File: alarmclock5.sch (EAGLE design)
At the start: 38 parts, among them X1 MKDSN1,5/2-5,08, X2 MKDSN1,5/2-5,08, X3 MKDSN1,5/2-5,08, X4 MKDSN1,5/2-5,08, X5 MKDSN1,5/2-5,08

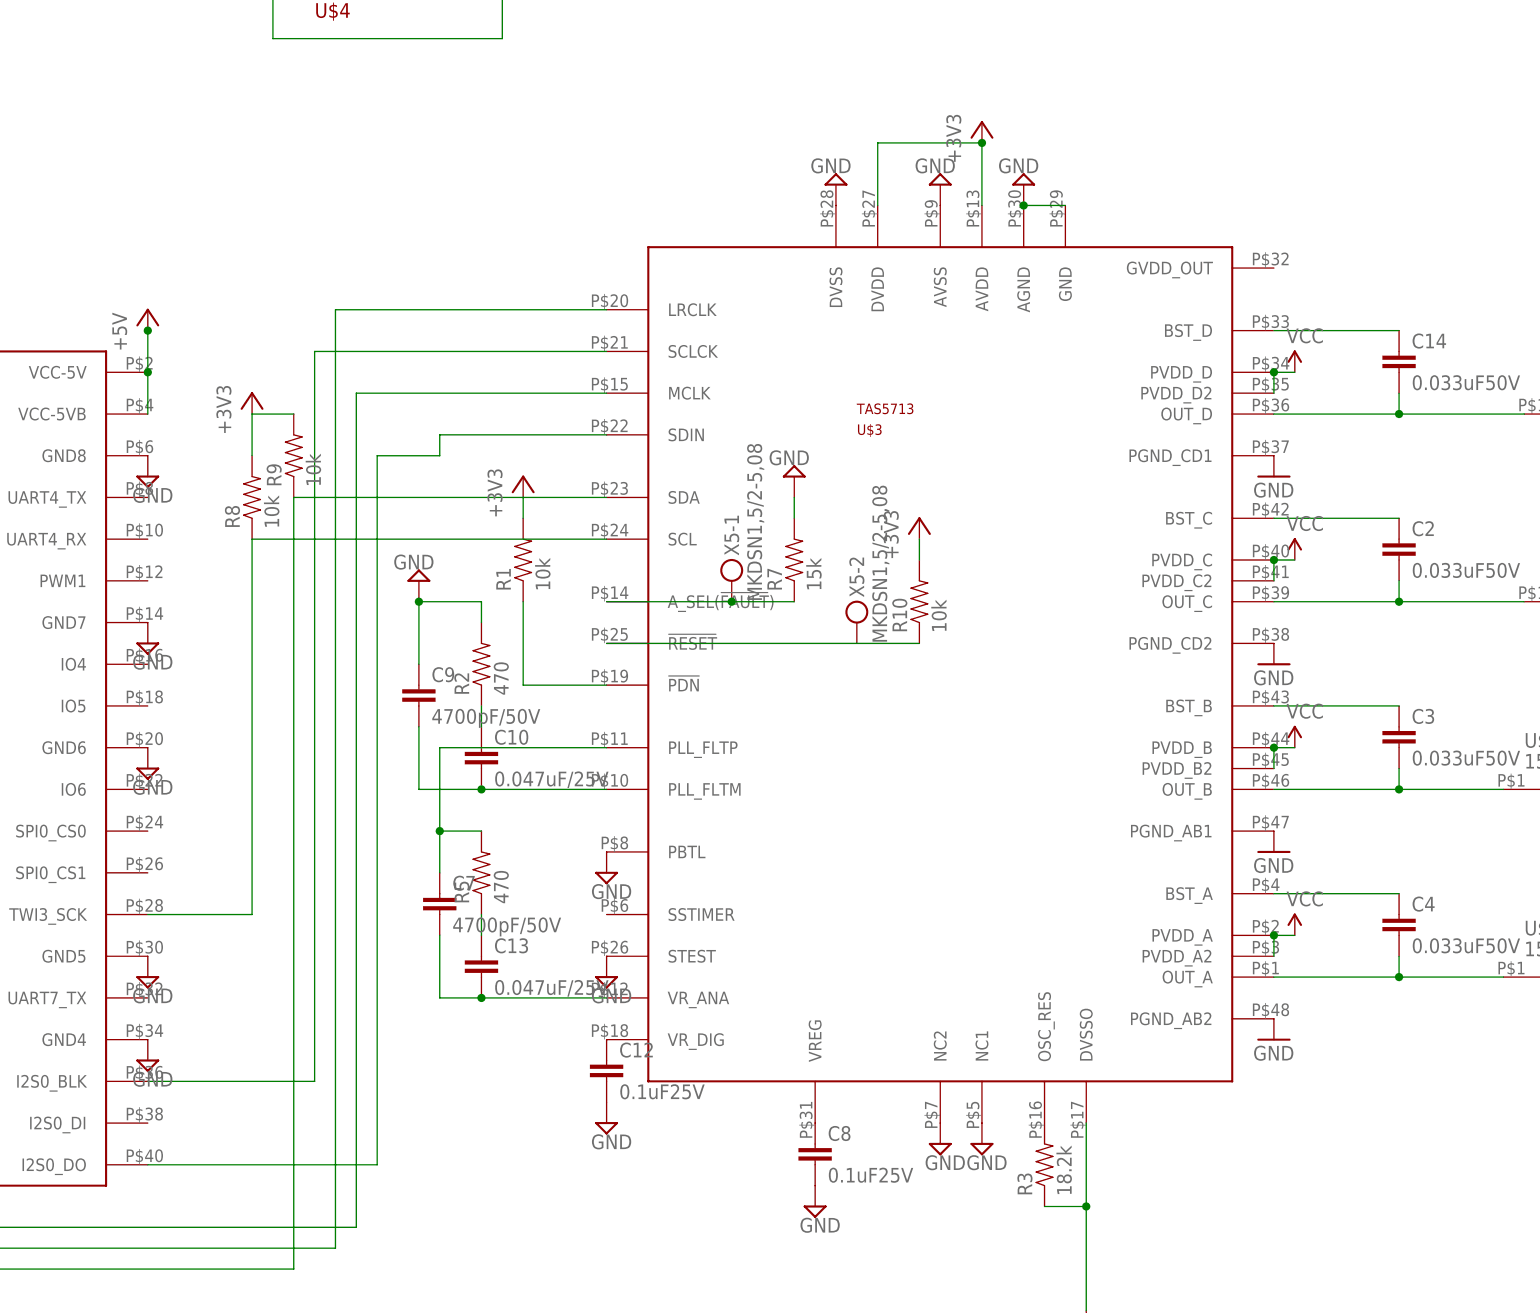
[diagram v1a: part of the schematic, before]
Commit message: new board with RESET and PDN accessible via GPIO
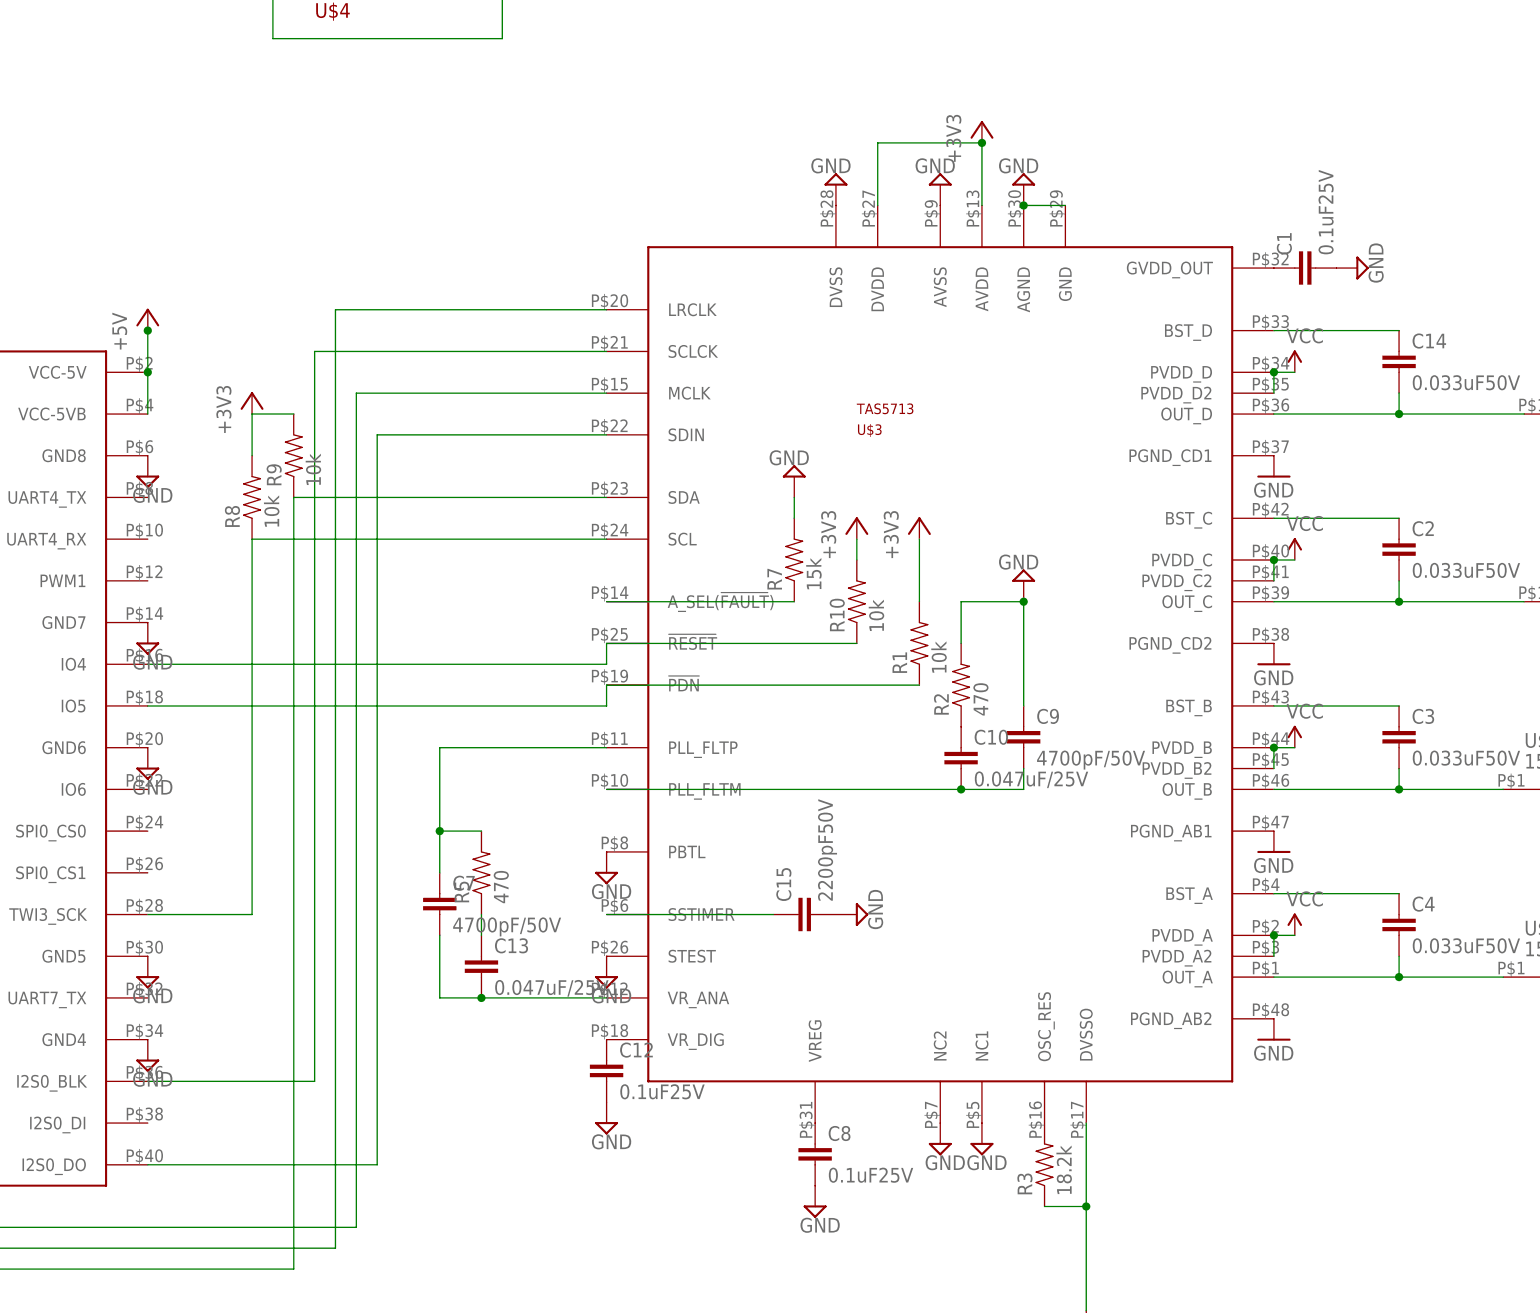
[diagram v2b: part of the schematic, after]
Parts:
- removed X5: MKDSN1,5/2-5,08, con-phoenix-508:MKDSN1,5/2-5,08
- added C1: 0.1uF25V, SparkFun-Capacitors:CAP0603-CAP
- added C15: 2200pF50V, SparkFun-Capacitors:CAP0603-CAP
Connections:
- new net N$38: C1.1, U$3.GVDD_OUT
- new net N$39: C15.1, U$3.SSTIMER
- net GND: now also C1.2, C15.2
- net N$28: now also U$5.IO5
- net N$34: no longer X5-1.KL
- net N$37: now also U$5.IO4; no longer X5-2.KL
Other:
- moved on the sheet: C10, C9, R1, R10, R2
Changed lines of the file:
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@@
 <part name="R9" library="SparkFun-Passives" deviceset="RESISTOR" device="0603-RES" value="10k"/>
 <part name="+3V8" library="supply1" deviceset="+3V3" device=""/>
-<part name="X5" library="con-phoenix-508" deviceset="MKDSN1,5/2-5,08" device=""/>
 <part name="R10" library="SparkFun-Passives" deviceset="RESISTOR" device="0603-RES" value="10k"/>
+<part name="C1" library="SparkFun-Capacitors" deviceset="CAP" device="0603-CAP" value="0.1uF25V"/>
+<part name="SUPPLY18" library="supply2" deviceset="GND" device=""/>
+<part name="C15" library="SparkFun-Capacitors" deviceset="CAP" device="0603-CAP" value="2200pF50V"/>
+<part name="SUPPLY30" library="supply2" deviceset="GND" device=""/>
 </parts>
 <sheets>
@@
 <instance part="C12" gate="G$1" x="76.2" y="-68.58"/>
 <instance part="C13" gate="G$1" x="60.96" y="-55.88"/>
-<instance part="C10" gate="G$1" x="60.96" y="-30.48"/>
+<instance part="C10" gate="G$1" x="119.38" y="-30.48"/>
 <instance part="C7" gate="G$1" x="55.88" y="-48.26"/>
-<instance part="C9" gate="G$1" x="53.34" y="-22.86"/>
+<instance part="C9" gate="G$1" x="127" y="-27.94"/>
 <instance part="R5" gate="G$1" x="60.96" y="-43.18" rot="R90"/>
-<instance part="R2" gate="G$1" x="60.96" y="-17.78" rot="R90"/>
+<instance part="R2" gate="G$1" x="119.38" y="-20.32" rot="R90"/>
 <instance part="R3" gate="G$1" x="129.54" y="-78.74" rot="R90"/>
-<instance part="R1" gate="G$1" x="66.04" y="-5.08" rot="R90"/>
+<instance part="R1" gate="G$1" x="114.3" y="-15.24" rot="R90"/>
 <instance part="C11" gate="G$1" x="73.66" y="76.2"/>
-<instance part="SUPPLY6" gate="GND" x="53.34" y="-7.62" rot="R180"/>
+<instance part="SUPPLY6" gate="GND" x="127" y="-7.62" rot="R180"/>
 <instance part="+3V1" gate="G$1" x="-20.32" y="27.94"/>
 <instance part="P+1" gate="1" x="20.32" y="25.4"/>
-<instance part="+3V2" gate="G$1" x="66.04" y="5.08"/>
+<instance part="+3V2" gate="G$1" x="114.3" y="0"/>
 <instance part="+3V3" gate="G$1" x="121.92" y="48.26"/>
 <instance part="SUPPLY7" gate="GND" x="104.14" y="40.64" rot="R180"/>
@@
 <instance part="SUPPLY25" gate="GND" x="121.92" y="-76.2"/>
 <instance part="SUPPLY26" gate="GND" x="134.62" y="-99.06"/>
-<instance part="+3V4" gate="G$1" x="114.3" y="0"/>
+<instance part="+3V4" gate="G$1" x="106.68" y="0"/>
 <instance part="X3" gate="-1" x="-68.58" y="-7.62" rot="R180"/>
 <instance part="X3" gate="-2" x="-68.58" y="-12.7" rot="R180"/>
@@
 <instance part="R9" gate="G$1" x="38.1" y="7.62" rot="R90"/>
 <instance part="+3V8" gate="G$1" x="33.02" y="15.24"/>
-<instance part="X5" gate="-1" x="91.44" y="-7.62" rot="R90"/>
-<instance part="X5" gate="-2" x="106.68" y="-12.7" rot="R90"/>
-<instance part="R10" gate="G$1" x="114.3" y="-10.16" rot="R90"/>
+<instance part="R10" gate="G$1" x="106.68" y="-10.16" rot="R90"/>
+<instance part="C1" gate="G$1" x="162.56" y="30.48" rot="R90"/>
+<instance part="SUPPLY18" gate="GND" x="167.64" y="30.48" rot="R90"/>
+<instance part="C15" gate="G$1" x="101.6" y="-48.26" rot="R90"/>
+<instance part="SUPPLY30" gate="GND" x="106.68" y="-48.26" rot="R90"/>
 </instances>
 <busses>
@@
 </segment>
 <segment>
-<wire x1="53.34" y1="-17.78" x2="53.34" y2="-10.16" width="0.1524" layer="91"/>
-<wire x1="60.96" y1="-12.7" x2="60.96" y2="-10.16" width="0.1524" layer="91"/>
-<wire x1="60.96" y1="-10.16" x2="53.34" y2="-10.16" width="0.1524" layer="91"/>
+<wire x1="127" y1="-22.86" x2="127" y2="-10.16" width="0.1524" layer="91"/>
+<wire x1="119.38" y1="-15.24" x2="119.38" y2="-10.16" width="0.1524" layer="91"/>
+<wire x1="119.38" y1="-10.16" x2="127" y2="-10.16" width="0.1524" layer="91"/>
 <pinref part="C9" gate="G$1" pin="1"/>
 <pinref part="R2" gate="G$1" pin="2"/>
 <pinref part="SUPPLY6" gate="GND" pin="GND"/>
-<junction x="53.34" y="-10.16"/>
+<junction x="127" y="-10.16"/>
 </segment>
 <segment>
@@
 <wire x1="99.06" y1="0" x2="99.06" y2="2.54" width="0.1524" layer="91"/>
 </segment>
+<segment>
+<pinref part="C1" gate="G$1" pin="2"/>
+<pinref part="SUPPLY18" gate="GND" pin="GND"/>
+</segment>
+<segment>
+<pinref part="C15" gate="G$1" pin="2"/>
+<pinref part="SUPPLY30" gate="GND" pin="GND"/>
+</segment>
 </net>
 <net name="N$1" class="0">
@@
 <pinref part="U$5" gate="G$1" pin="I2S0_DO"/>
 <wire x1="20.32" y1="-78.74" x2="48.26" y2="-78.74" width="0.1524" layer="91"/>
-<wire x1="48.26" y1="-78.74" x2="48.26" y2="7.62" width="0.1524" layer="91"/>
+<wire x1="48.26" y1="-78.74" x2="48.26" y2="10.16" width="0.1524" layer="91"/>
 <pinref part="U$3" gate="G$1" pin="SDIN"/>
-<wire x1="55.88" y1="10.16" x2="76.2" y2="10.16" width="0.1524" layer="91"/>
-<wire x1="55.88" y1="10.16" x2="55.88" y2="7.62" width="0.1524" layer="91"/>
-<wire x1="55.88" y1="7.62" x2="48.26" y2="7.62" width="0.1524" layer="91"/>
+<wire x1="48.26" y1="10.16" x2="76.2" y2="10.16" width="0.1524" layer="91"/>
 </segment>
 </net>
@@
 <segment>
 <pinref part="U$3" gate="G$1" pin="PLL_FLTM"/>
-<wire x1="76.2" y1="-33.02" x2="60.96" y2="-33.02" width="0.1524" layer="91"/>
-<wire x1="60.96" y1="-33.02" x2="53.34" y2="-33.02" width="0.1524" layer="91"/>
-<wire x1="53.34" y1="-25.4" x2="53.34" y2="-33.02" width="0.1524" layer="91"/>
+<wire x1="76.2" y1="-33.02" x2="119.38" y2="-33.02" width="0.1524" layer="91"/>
+<wire x1="119.38" y1="-33.02" x2="127" y2="-33.02" width="0.1524" layer="91"/>
+<wire x1="127" y1="-30.48" x2="127" y2="-33.02" width="0.1524" layer="91"/>
 <pinref part="C10" gate="G$1" pin="2"/>
-<junction x="60.96" y="-33.02"/>
+<junction x="119.38" y="-33.02"/>
 <pinref part="C9" gate="G$1" pin="2"/>
 </segment>
@@
 <net name="N$25" class="0">
 <segment>
-<wire x1="60.96" y1="-22.86" x2="60.96" y2="-25.4" width="0.1524" layer="91"/>
 <pinref part="C10" gate="G$1" pin="1"/>
 <pinref part="R2" gate="G$1" pin="1"/>
@@
 <segment>
 <pinref part="U$3" gate="G$1" pin="!PDN!"/>
-<wire x1="76.2" y1="-20.32" x2="66.04" y2="-20.32" width="0.1524" layer="91"/>
-<wire x1="66.04" y1="-20.32" x2="66.04" y2="-10.16" width="0.1524" layer="91"/>
+<wire x1="76.2" y1="-20.32" x2="114.3" y2="-20.32" width="0.1524" layer="91"/>
 <pinref part="R1" gate="G$1" pin="1"/>
+<pinref part="U$5" gate="G$1" pin="IO5"/>
+<wire x1="20.32" y1="-22.86" x2="76.2" y2="-22.86" width="0.1524" layer="91"/>
+<wire x1="76.2" y1="-22.86" x2="76.2" y2="-20.32" width="0.1524" layer="91"/>
 </segment>
 </net>
@@
 <segment>
 <pinref part="+3V2" gate="G$1" pin="+3V3"/>
-<wire x1="66.04" y1="0" x2="66.04" y2="2.54" width="0.1524" layer="91"/>
+<wire x1="114.3" y1="-10.16" x2="114.3" y2="-2.54" width="0.1524" layer="91"/>
 <pinref part="R1" gate="G$1" pin="2"/>
 </segment>
@@
 <pinref part="R10" gate="G$1" pin="2"/>
 <pinref part="+3V4" gate="G$1" pin="+3V3"/>
-<wire x1="114.3" y1="-5.08" x2="114.3" y2="-2.54" width="0.1524" layer="91"/>
+<wire x1="106.68" y1="-5.08" x2="106.68" y2="-2.54" width="0.1524" layer="91"/>
 </segment>
 </net>
@@
 <segment>
 <pinref part="R7" gate="G$1" pin="1"/>
-<wire x1="99.06" y1="-10.16" x2="91.44" y2="-10.16" width="0.1524" layer="91"/>
 <pinref part="U$3" gate="G$1" pin="A_SEL(!FAULT!)"/>
-<wire x1="91.44" y1="-10.16" x2="76.2" y2="-10.16" width="0.1524" layer="91"/>
-<pinref part="X5" gate="-1" pin="KL"/>
-<junction x="91.44" y="-10.16"/>
+<wire x1="99.06" y1="-10.16" x2="76.2" y2="-10.16" width="0.1524" layer="91"/>
 </segment>
 </net>
@@
 <segment>
 <pinref part="U$3" gate="G$1" pin="!RESET!"/>
-<pinref part="X5" gate="-2" pin="KL"/>
 <wire x1="106.68" y1="-15.24" x2="76.2" y2="-15.24" width="0.1524" layer="91"/>
 <pinref part="R10" gate="G$1" pin="1"/>
-<wire x1="106.68" y1="-15.24" x2="114.3" y2="-15.24" width="0.1524" layer="91"/>
-</segment>
-</net>
+<pinref part="U$5" gate="G$1" pin="IO4"/>
+<wire x1="20.32" y1="-17.78" x2="76.2" y2="-17.78" width="0.1524" layer="91"/>
+<wire x1="76.2" y1="-17.78" x2="76.2" y2="-15.24" width="0.1524" layer="91"/>
+</segment>
+</net>
+<net name="N$38" class="0">
+<segment>
+<pinref part="U$3" gate="G$1" pin="GVDD_OUT"/>
+<pinref part="C1" gate="G$1" pin="1"/>
+</segment>
+</net>
+<net name="N$39" class="0">
+<segment>
+<pinref part="U$3" gate="G$1" pin="SSTIMER"/>
+<pinref part="C15" gate="G$1" pin="1"/>
+<wire x1="76.2" y1="-48.26" x2="96.52" y2="-48.26" width="0.1524" layer="91"/>
+</segment>
+</net>
